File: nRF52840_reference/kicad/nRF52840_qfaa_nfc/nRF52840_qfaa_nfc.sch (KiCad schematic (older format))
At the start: 1 part

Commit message: Update KiCAD Project nRF52840_qfaa_nfc
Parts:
- added AE1: Antenna, Nordic_misc:Nordic_misc-QWMP_BEND_LEFT_+0, symbol Antenna
- added C1, C10, C11, C12, C13, C14, C15, C16, C17, C18, C19, C2, C20, C21, C3, C4, C5, C6, C7, C8, C9: C, Nordic_misc:C_0402, symbol C
- added J1: CONN_COAXIAL, Nordic_misc:Nordic_misc-MM8130-2600, symbol CONN_COAXIAL
- added L1, L2, L3, L4: L, Nordic_misc:L_0402, symbol L
- added X1: XTAL_32MHZ, Nordic_nRF:Crystal_SMD_2016-4pin_2.0x1.6mm, symbol XTAL_32MHZ
- added X2: XTAL_32KHZ, Nordic_nRF:Crystal_SMD_3215-2pin_3.2x1.5mm, symbol XTAL_32KHZ
- U1: renamed from U?; footprint (none) -> Nordic_nRF:AQFN73_7x7mm
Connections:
- net GND: now also U1.F23 (VSS_PA), C1.1, C10.1, C11.1, C12.2, C13.2, C14.2, C15.2, C18.1, C19.1, C2.1, C20.1, C21.1, C3.1, C4.1, C5.2, C6.1, C7.1, C8.1, C9.1, X1.2, X1.4
- net at U1.A18 (DEC2): now also C13.1
- net +3V3: now reaches U1.A22 (VDD)
- net +3V3: now also U1.AD14 (VDD), U1.AD2 (VBUS), U1.AD23 (VDD), U1.B1 (VDD), U1.W1 (VDD), C12.1, C14.1, C20.2, C6.2, C7.2, C8.2, L4.1
- net at U1.A23 (XC2): now also C2.2, X1.1
- net SWDCLK: now reaches U1.AA24 (SWDCLK)
- net at U1.AB2 (DCCH): now also L4.2
- net SWDIO: now reaches U1.AC24 (SWDIO)
- net at U1.AC5 (DECUSB): now also C19.2
- net at U1.B24 (XC1): now also C1.2, X1.3
- net at U1.B3 (DCC): now also L2.2
- net at U1.B5 (DEC4): now also C15.1, L3.1
- net at U1.C1 (DEC1): now also C5.1
- net at U1.D23 (DEC3): now also C11.2
- net at U1.E24 (DEC6): now also C10.2
- net at U1.H23 (ANT): now also C3.2, L1.1
- net at U1.N24 (DEC): now also C9.2
- net VDD: now reaches U1.Y2 (VDDH)
- net VDD: now also C18.2
- net P0.00/XL1: no longer names the net of U1.D2 (P0.00/XL1)
- net P0.00/XL1: now also C16.1
- net P0.01/XL2: no longer names the net of U1.F2 (P0.01/XL2)
- net P0.01/XL2: now also C17.1
- new net: C16.2, X2.1
- new net: C17.2, X2.2
- new net: L2.1, L3.2
- new net: C4.2, J1.1 (In), L1.2
- new net: AE1.1 (A), C21.2, J1.2 (Ext)
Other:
- moved on the sheet: U1

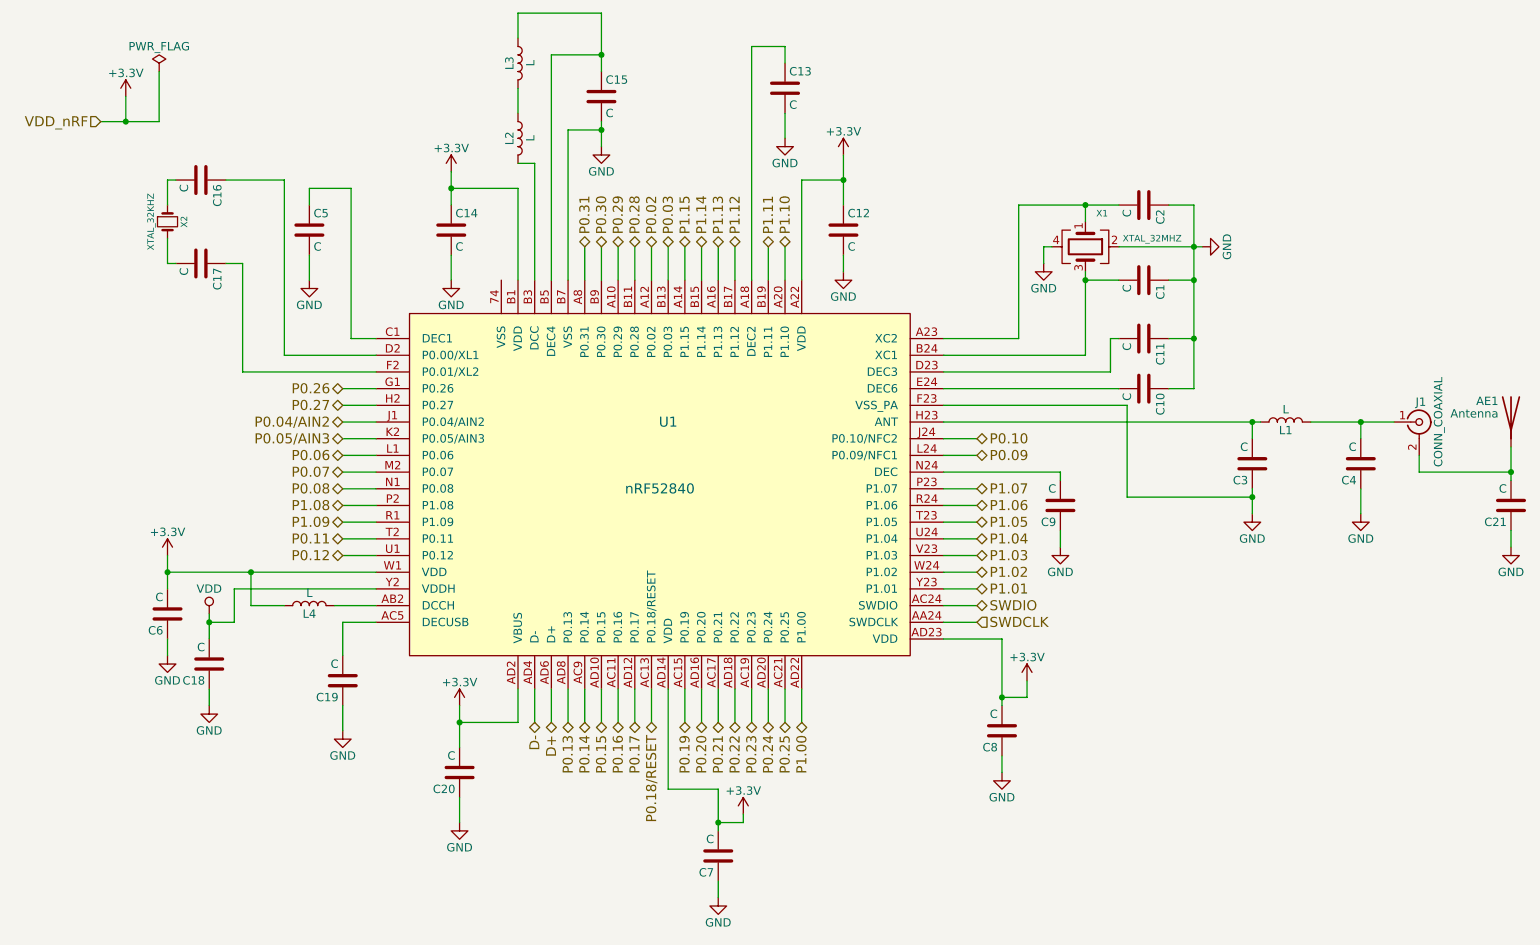
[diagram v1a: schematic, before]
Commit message: Update KiCAD project nRF52840_qfaa_nfc
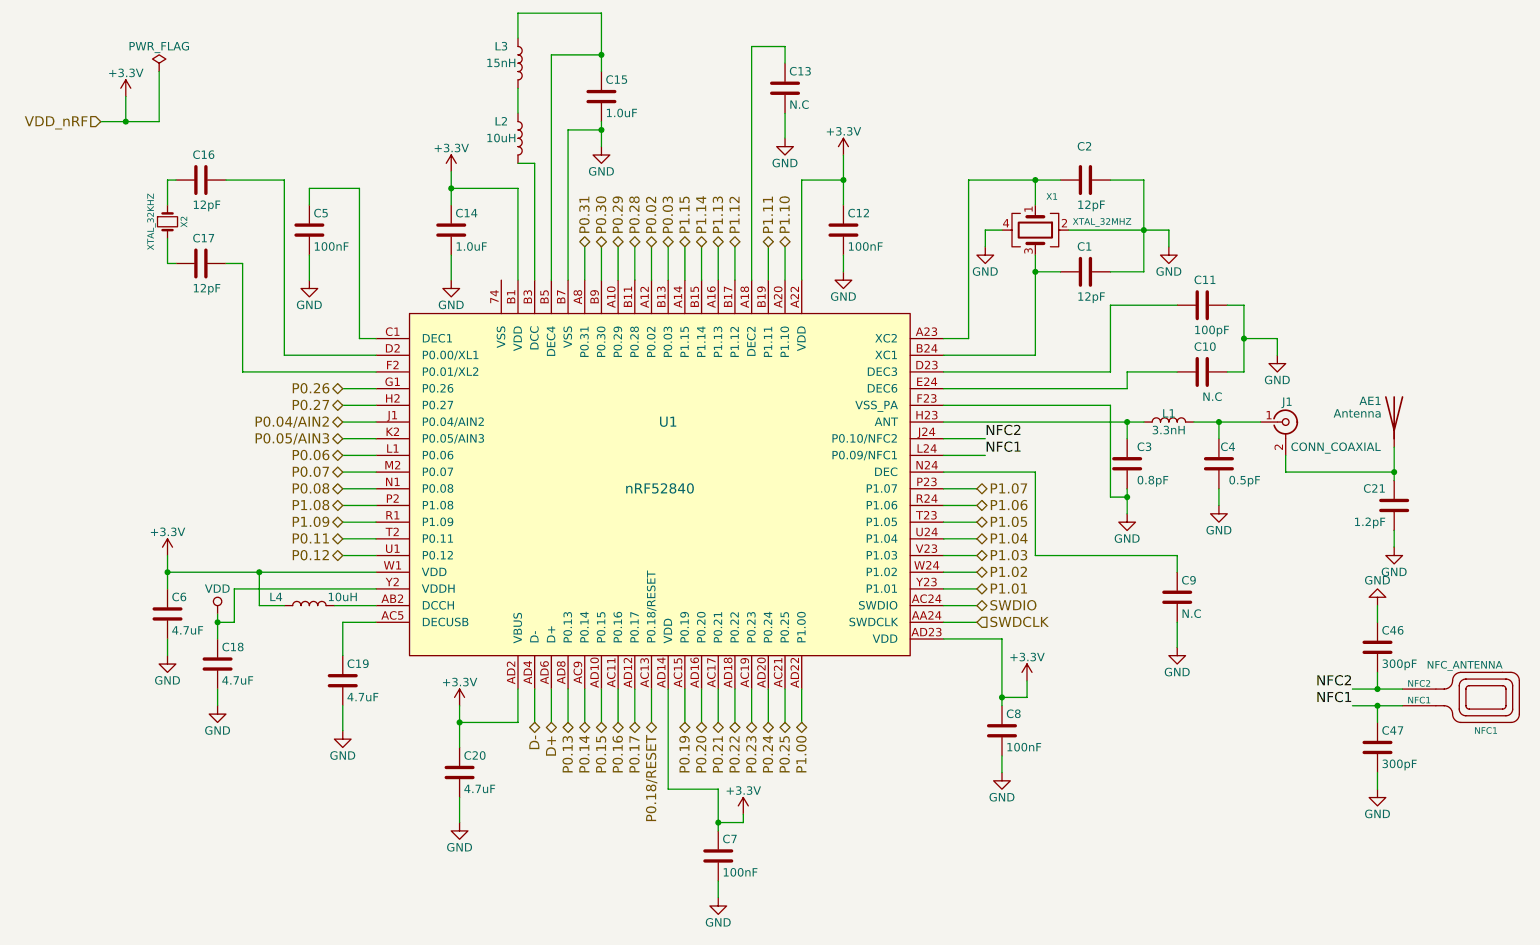
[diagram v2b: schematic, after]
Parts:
- added C46, C47: 300pF, Nordic_misc:C_0402, symbol C
- added NFC1: NFC_ANTENNA, Nordic_misc:Nordic_misc-NFC_ANT, symbol NFC_ANTENNA
- C1, C16, C17, C2: value C -> 12pF
- C10, C13, C9: value C -> N.C
- C11: value C -> 100pF
- C12, C5, C7, C8: value C -> 100nF
- C14, C15: value C -> 1.0uF; footprint Nordic_misc:C_0402 -> Nordic_misc:C_0603
- C18, C19, C20, C6: value C -> 4.7uF; footprint Nordic_misc:C_0402 -> Nordic_misc:C_0603
- C21: value C -> 1.2pF
- C3: value C -> 0.8pF
- C4: value C -> 0.5pF
- L1: value L -> 3.3nH; footprint Nordic_misc:L_0402 -> Nordic_misc:L_0603
- L2, L4: value L -> 10uH; footprint Nordic_misc:L_0402 -> Nordic_misc:L_0603
- L3: value L -> 15nH
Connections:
- net +3V3: now also C20.1, C6.1, C7.1, C8.1; no longer C20.2, C6.2, C7.2, C8.2
- net GND: now also C18.2, C19.2, C20.2, C6.2, C7.2, C8.2, C9.2, C46.1, C47.2; no longer C18.1, C19.1, C20.1, C6.1, C7.1, C8.1, C9.1
- net VDD: now also C18.1; no longer C18.2
- net at U1.AC5 (DECUSB): now also C19.1; no longer C19.2
- net at U1.N24 (DEC): now also C9.1; no longer C9.2
- net P0.09 renamed NFC1
- net NFC1: now also C47.1, NFC1.2 (NFC1)
- net P0.10 renamed NFC2
- net NFC2: now also C46.2, NFC1.1 (NFC2)
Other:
- moved on the sheet: AE1, C1, C10, C11, C18, C2, C21, C3, C4, C9, J1, L1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

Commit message: Update KiCAD Project nRF52840_qfaa_nfc
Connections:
- net GND: now also U1.74 (VSS)
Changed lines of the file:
@@
 Text Label 8600 5000 2    60   ~ 0
 NFC2
+Wire Wire Line
+	3500 2550 3500 2450
+Wire Wire Line
+	3500 2450 3200 2450
+Connection ~ 3200 2450
 $EndSCHEMATC
